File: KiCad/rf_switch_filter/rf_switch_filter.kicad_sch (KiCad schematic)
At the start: 15 parts, among them J10 FILTER_OUT, J9 ANT, U17 BPF-A355, U3 SKY13588-460LF, U4 SKY13588-460LF, U5 SN74AVC2T244DQER, U6 MIC5365-1.8YC5-TR, U7 MIC5365-3.3YC5-TR

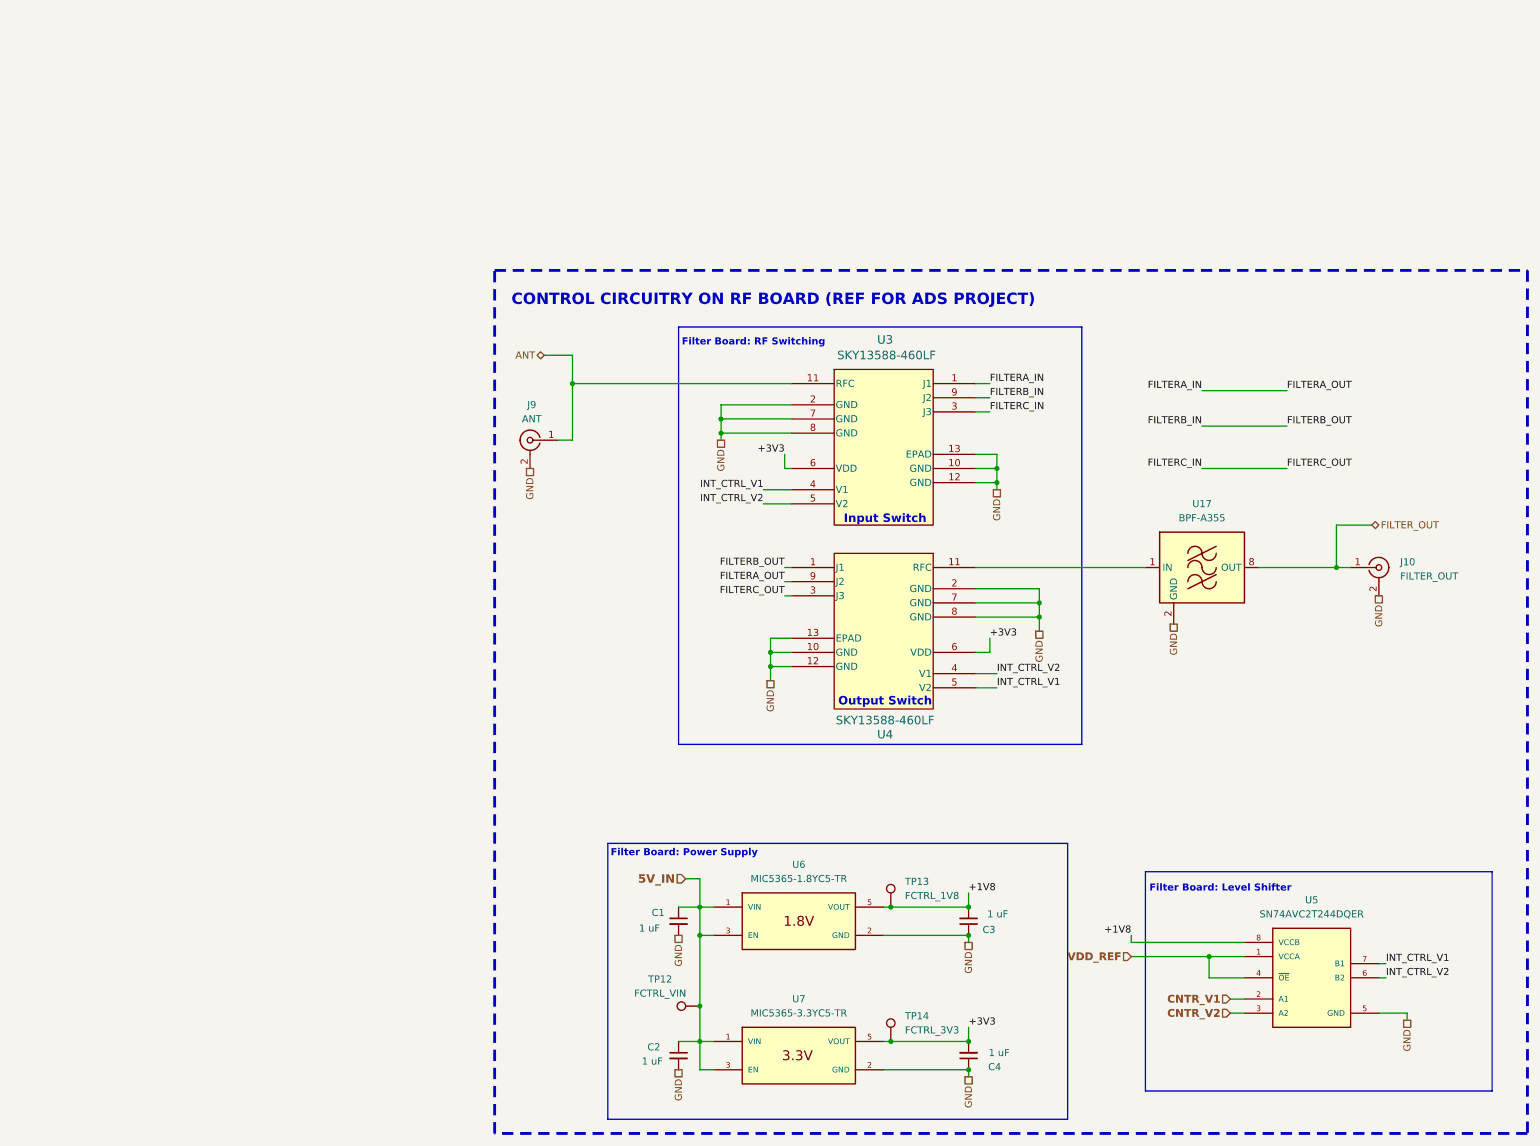
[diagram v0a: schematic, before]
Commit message: Fix up RF switch project
Laid out schematic to be more legible, added screw terminals from wiring
diagram, changed GND symbols, changed labels to be global labels, and
added project libraries
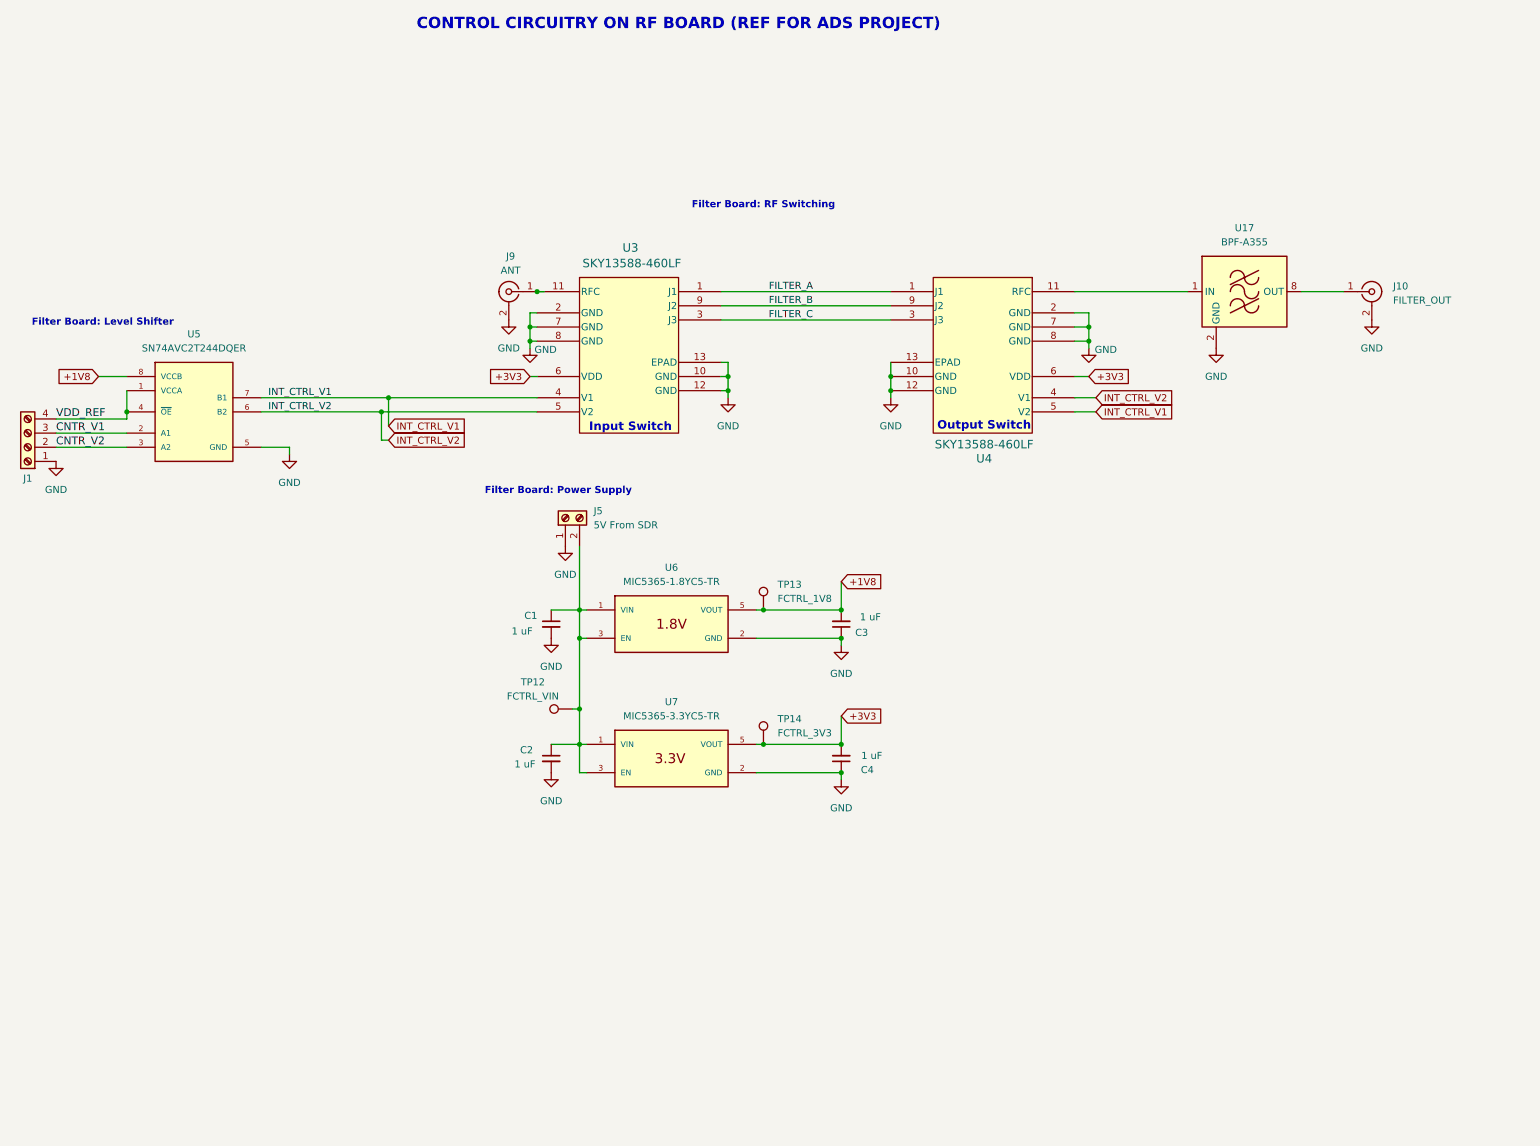
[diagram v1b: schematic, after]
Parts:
- added J1: (no value), Library:PHOENIX_1729144, symbol Connector:Screw_Terminal_01x04
- added J5: 5V From SDR, Library:CONN_1729128_PXC, symbol Connector:Screw_Terminal_01x02
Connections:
- net CNTR_V1: now also J1.3 (Pin_3)
- net CNTR_V2: now also J1.2 (Pin_2)
- net GND: now also J1.1 (Pin_1), J5.1 (Pin_1)
- net VDD_REF: now also J1.4 (Pin_4)
- net 5V_IN: no longer names the net of C1.1, C2.1, TP12.1, U6.1 (VIN), U6.3 (EN), U7.1 (VIN), U7.3 (EN)
- net 5V_IN: now also J5.2 (Pin_2)
- net ANT: no longer names the net of J9.1 (In), U3.11 (RFC)
- net FILTERA_IN renamed FILTER_A
- net FILTER_A: now also U4.1 (J1); no longer U4.9 (J2)
- net FILTERB_IN renamed FILTER_B
- net FILTER_B: now also U4.9 (J2); no longer U4.1 (J1)
- net FILTERC_IN renamed FILTER_C
- net FILTER_OUT: no longer names the net of J10.1 (In), U17.8 (OUT)
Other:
- moved on the sheet: C1, C2, C3, C4, J10, J9, TP12, TP13, TP14, U17, U3, U4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
